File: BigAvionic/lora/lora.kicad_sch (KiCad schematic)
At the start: 0 parts

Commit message: add new power layer
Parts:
- added C43, C45: 100n, Capacitor_SMD:C_0805_2012Metric_Pad1.18x1.45mm_HandSolder, symbol Device:C
- added C44: 100u, Capacitor_SMD:C_0805_2012Metric_Pad1.18x1.45mm_HandSolder, symbol Device:C
- added C46: 22u, Capacitor_SMD:C_0805_2012Metric_Pad1.18x1.45mm_HandSolder, symbol Device:C
- added H1, H2, H3, H4: MountingHole, MountingHole:MountingHole_3.2mm_M3_DIN965_Pad, symbol Mechanical:MountingHole
- added R30, R31: 22ohm, Resistor_SMD:R_0805_2012Metric_Pad1.20x1.40mm_HandSolder, symbol Device:R
- added R32, R33: 10k, Resistor_SMD:R_0805_2012Metric_Pad1.20x1.40mm_HandSolder, symbol Device:R
- added U10: E22-400T30S, Tony:XCVR_E22-900T30S, symbol A_library:E22-XXXT30
- added U11: E80-900M23313S, Tony:E80-xxxM2213S, symbol A_library:E80-xxxM2213S
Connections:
- new net: R31.1, U10.4 (TXD)
- new net: R30.1, U10.5 (RXD)
- new net +3.3V: C43.1, C44.1, C45.1, C46.1, R32.2, R33.2, U10.2 (VCC), U11.25 (VCC)
- new net CSB_LORA920: U11.6 (NSS)
- new net GND: C43.2, C44.2, C45.2, C46.2, U10.1 (GND), U10.12 (GND), U10.13 (GND), U10.14 (GND), U10.23 (GND), U11.1 (GND), U11.19 (GND), U11.26 (GND), U11.8 (GND)
- new net LORA433_BUSY: U10.3 (AUX)
- new net LORA433_M0: U10.7 (M0)
- new net LORA433_M1: U10.6 (M1)
- new net LORA433_RST: R32.1, U10.22 (RESET)
- new net LORA920_BUSY: U11.7 (BUSY)
- new net LORA920_INT: U11.22 (DIO9)
- new net LORA920_RST: R33.1, U11.21 (LR_NRST)
- new net SPI3_MISO: U11.3 (MISO)
- new net SPI3_MOSI: U11.4 (MOSI)
- new net SPI3_SCK: U11.5 (SCK)
- new net UART3_RX: R31.2
- new net UART3_TX: R30.2
- no-connect marks 0 -> 8
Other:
- note added: "LORA 433"
- note added: "LORA 920"
- note added: "using ipx in the lora model"

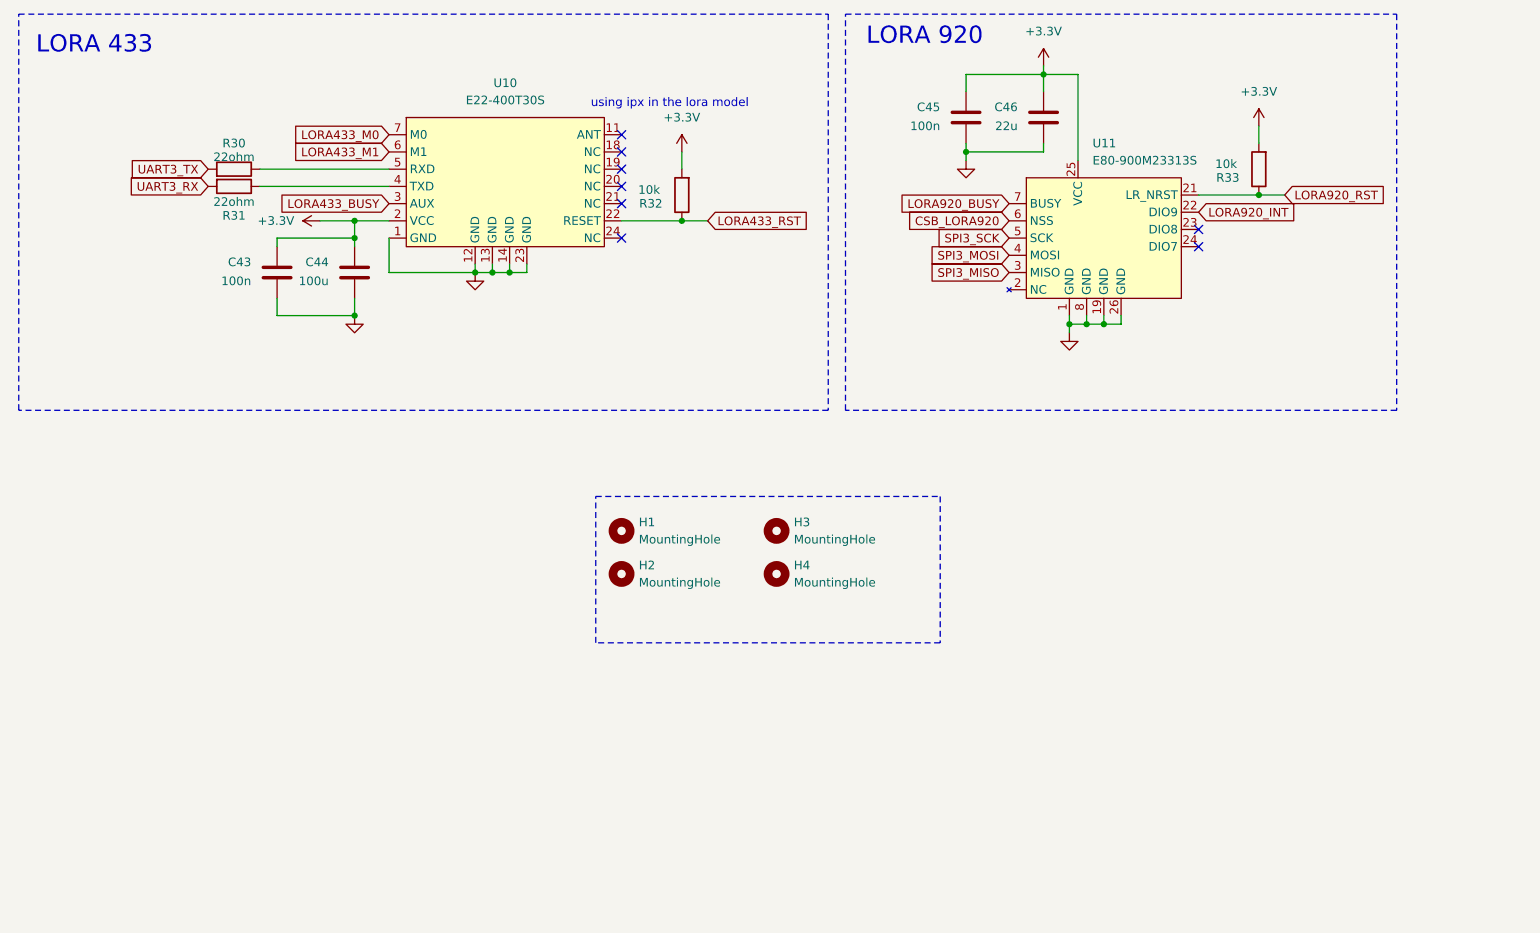
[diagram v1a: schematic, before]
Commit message: finish lora layer
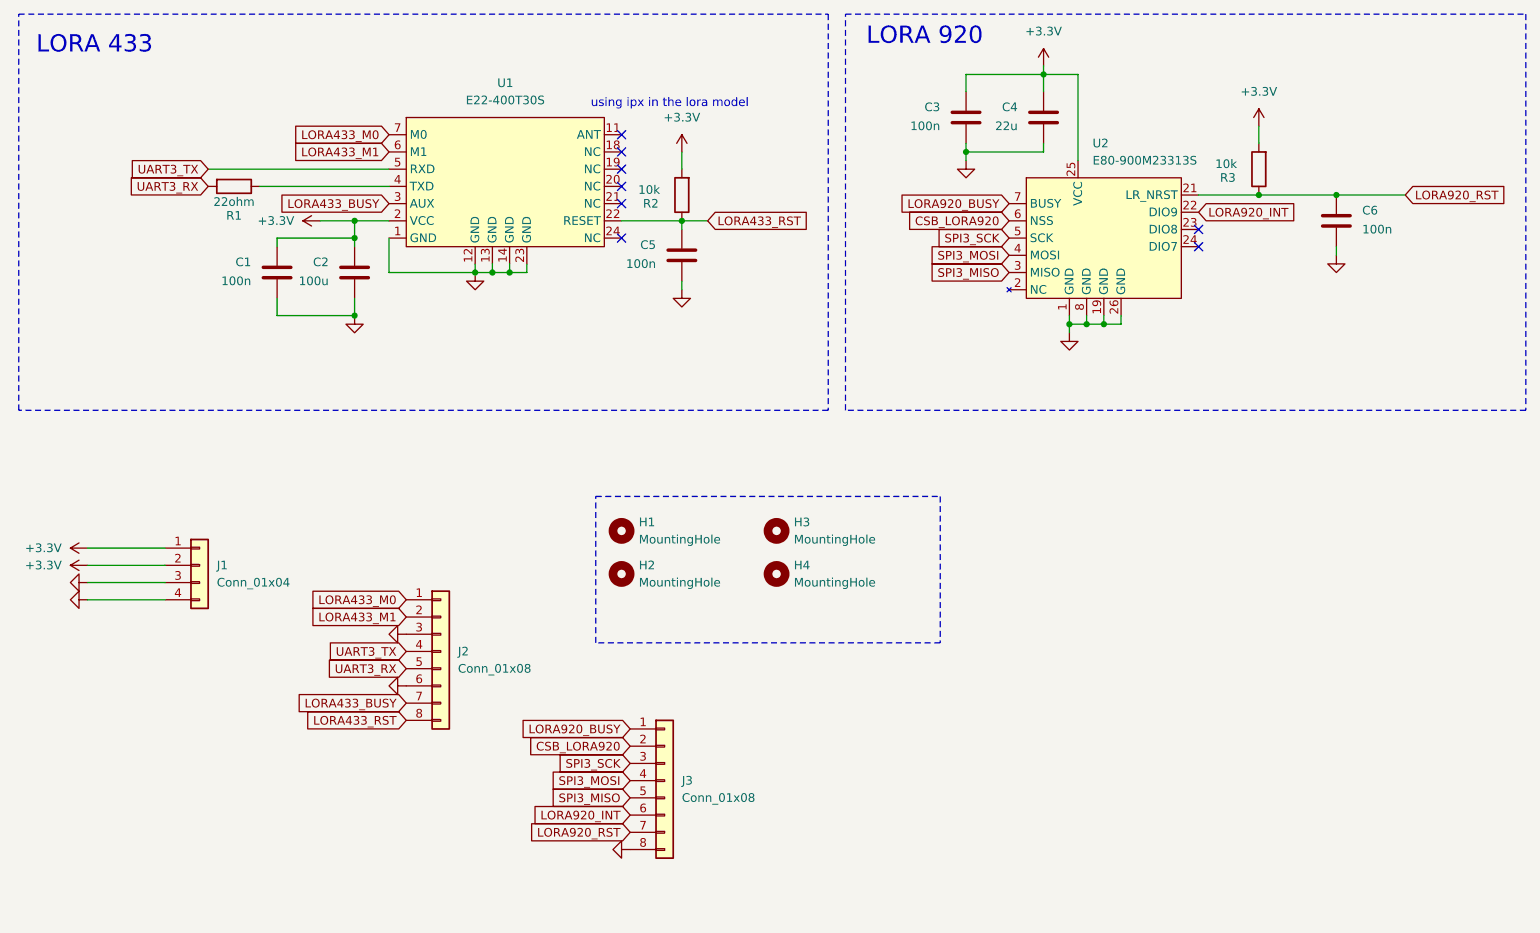
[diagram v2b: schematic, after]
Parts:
- removed R30: 22ohm, Resistor_SMD:R_0805_2012Metric_Pad1.20x1.40mm_HandSolder, symbol Device:R
- added C5, C6: 100n, Capacitor_SMD:C_0805_2012Metric_Pad1.18x1.45mm_HandSolder, symbol Device:C
- added J1: Conn_01x04, Connector_JST:JST_GH_SM04B-GHS-TB_1x04-1MP_P1.25mm_Horizontal, symbol Connector_Generic:Conn_01x04
- added J2, J3: Conn_01x08, Connector_JST:JST_GH_SM08B-GHS-TB_1x08-1MP_P1.25mm_Horizontal, symbol Connector_Generic:Conn_01x08
- renumbered C43 to C1, C44 to C2, C45 to C3, C46 to C4, R31 to R1, R32 to R2, R33 to R3, U10 to U1, U11 to U2
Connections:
- net +3.3V: now also J1.1 (Pin_1), J1.2 (Pin_2)
- net CSB_LORA920: now also J3.2 (Pin_2)
- net GND: now also C5.2, C6.2, J1.3 (Pin_3), J1.4 (Pin_4), J2.3 (Pin_3), J2.6 (Pin_6), J3.8 (Pin_8)
- net LORA433_BUSY: now also J2.7 (Pin_7)
- net LORA433_M0: now also J2.1 (Pin_1)
- net LORA433_M1: now also J2.2 (Pin_2)
- net LORA433_RST: now also C5.1, J2.8 (Pin_8)
- net LORA920_BUSY: now also J3.1 (Pin_1)
- net LORA920_INT: now also J3.6 (Pin_6)
- net LORA920_RST: now also C6.1, J3.7 (Pin_7)
- net SPI3_MISO: now also J3.5 (Pin_5)
- net SPI3_MOSI: now also J3.4 (Pin_4)
- net SPI3_SCK: now also J3.3 (Pin_3)
- net UART3_RX: now also J2.5 (Pin_5)
- net UART3_TX: now also U1.5 (RXD), J2.4 (Pin_4)

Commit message: finish lora & top
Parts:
- added 3V3, GND1: TestPoint, TestPoint:TestPoint_Pad_D1.0mm, symbol Connector:TestPoint
- added D1: RED_LED, LED_SMD:LED_0805_2012Metric_Pad1.15x1.40mm_HandSolder, symbol Device:LED
- added R4: 1k, Resistor_SMD:R_0805_2012Metric_Pad1.20x1.40mm_HandSolder, symbol Device:R
- renumbered C5 to C3, C3 to C4, C4 to C5
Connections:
- net +3.3V: now also 3V3.1, R4.2
- net GND: now also D1.1 (K), GND1.1
- new net: D1.2 (A), R4.1
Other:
- note added: "connectors"
- note added: "testpoint/LED"
- moved on the sheet: H1, H2, H3, H4, J1, J2, J3

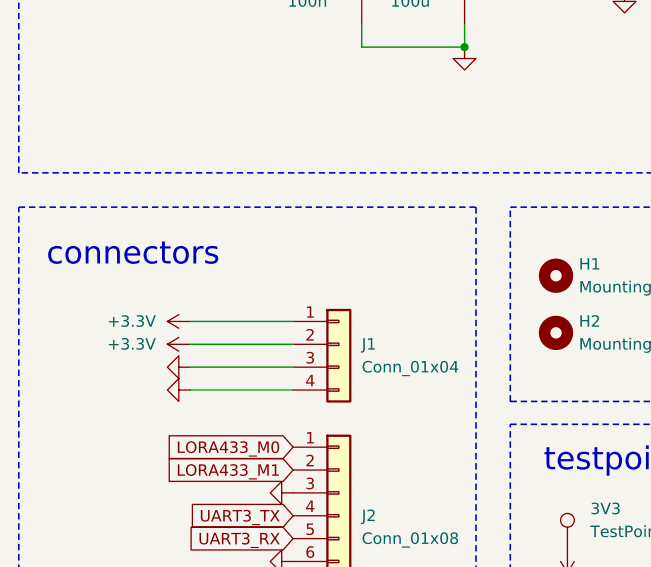
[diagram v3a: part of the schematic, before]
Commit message: check lora top power generate garber
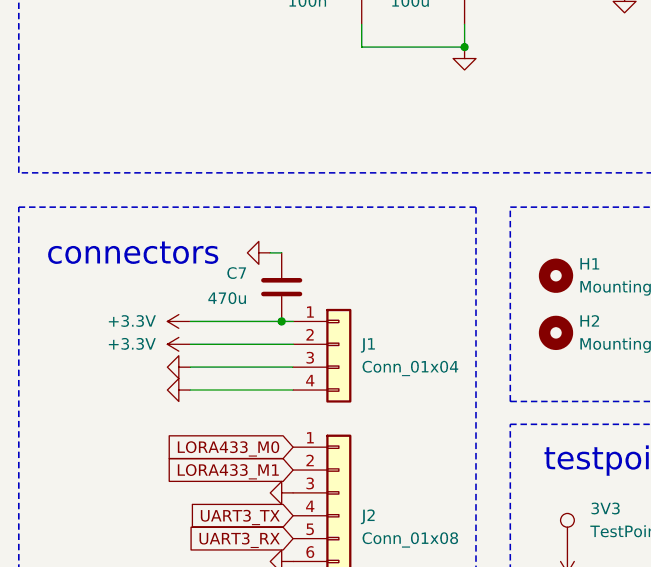
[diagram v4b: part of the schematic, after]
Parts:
- added C7: 470u, Capacitor_Tantalum_SMD:CP_EIA-7343-43_Kemet-X_HandSolder, symbol Device:C
- C2: footprint Capacitor_SMD:C_0805_2012Metric_Pad1.18x1.45mm_HandSolder -> Capacitor_Tantalum_SMD:CP_EIA-7343-31_Kemet-D_HandSolder
- C5: footprint Capacitor_SMD:C_0805_2012Metric_Pad1.18x1.45mm_HandSolder -> Capacitor_SMD:C_1206_3216Metric_Pad1.33x1.80mm_HandSolder
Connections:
- net +3.3V: now also C7.2
- net GND: now also C7.1
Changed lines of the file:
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@@
 	)
 	(junction
+		(at 78.74 134.62)
+		(diameter 0)
+		(color 0 0 0 0)
+	)
+	(junction
 		(at 99.06 90.17)
 		(diameter 0)
@@
 	(wire
 		(pts
-			(xy 80.01 134.62) (xy 68.58 134.62)
+			(xy 80.01 134.62) (xy 78.74 134.62)
 		)
 		(stroke
@@
 	(wire
 		(pts
+			(xy 77.47 127) (xy 78.74 127)
+		)
+		(stroke
+			(width 0)
+			(type default)
+		)
+	)
+	(wire
+		(pts
 			(xy 189.23 78.74) (xy 189.23 80.01)
 		)
@@
 	(wire
 		(pts
+			(xy 78.74 134.62) (xy 68.58 134.62)
+		)
+		(stroke
+			(width 0)
+			(type default)
+		)
+	)
+	(wire
+		(pts
 			(xy 104.14 97.79) (xy 116.84 97.79)
 		)
@@
 			)
 		)
-		(property "Footprint" "Capacitor_SMD:C_0805_2012Metric_Pad1.18x1.45mm_HandSolder"
+		(property "Footprint" "Capacitor_SMD:C_1206_3216Metric_Pad1.33x1.80mm_HandSolder"
 			(at 199.6948 78.74 0)
 			(effects
@@
 	)
 	(symbol
+		(lib_id "Device:C")
+		(at 78.74 130.81 0)
+		(mirror y)
+		(unit 1)
+		(exclude_from_sim no)
+		(in_bom yes)
+		(on_board yes)
+		(dnp no)
+		(property "Reference" "C7"
+			(at 74.93 129.286 0)
+			(effects
+				(font
+					(size 1.27 1.27)
+				)
+				(justify left)
+			)
+		)
+		(property "Value" "470u"
+			(at 74.93 132.0799 0)
+			(effects
+				(font
+					(size 1.27 1.27)
+				)
+				(justify left)
+			)
+		)
+		(property "Footprint" "Capacitor_Tantalum_SMD:CP_EIA-7343-43_Kemet-X_HandSolder"
+			(at 77.7748 134.62 0)
+			(effects
+				(font
+					(size 1.27 1.27)
+				)
+				(hide yes)
+			)
+		)
+		(property "Datasheet" "~"
+			(at 78.74 130.81 0)
+			(effects
+				(font
+					(size 1.27 1.27)
+				)
+				(hide yes)
+			)
+		)
+		(property "Description" "Unpolarized capacitor"
+			(at 78.74 130.81 0)
+			(effects
+				(font
+					(size 1.27 1.27)
+				)
+				(hide yes)
+			)
+		)
+		(pin "1"
+		)
+		(pin "2"
+		)
+		(instances
+			(project "lora"
+				(path "/e7e6f94f-519b-4ec5-b32e-6265e8eb4710"
+					(reference "C7")
+					(unit 1)
+				)
+			)
+		)
+	)
+	(symbol
 		(lib_id "power:GND")
 		(at 80.01 189.23 270)
@@
 	)
 	(symbol
+		(lib_id "power:GND")
+		(at 77.47 127 270)
+		(unit 1)
+		(exclude_from_sim no)
+		(in_bom yes)
+		(on_board yes)
+		(dnp no)
+		(property "Reference" "#PWR022"
+			(at 71.12 127 0)
+			(effects
+				(font
+					(size 1.27 1.27)
+				)
+				(hide yes)
+			)
+		)
+		(property "Value" "GND"
+			(at 72.39 127 0)
+			(effects
+				(font
+					(size 1.27 1.27)
+				)
+				(hide yes)
+			)
+		)
+		(property "Footprint" ""
+			(at 77.47 127 0)
+			(effects
+				(font
+					(size 1.27 1.27)
+				)
+				(hide yes)
+			)
+		)
+		(property "Datasheet" ""
+			(at 77.47 127 0)
+			(effects
+				(font
+					(size 1.27 1.27)
+				)
+				(hide yes)
+			)
+		)
+		(property "Description" "Power symbol creates a global label with name \"GND\" , ground"
+			(at 77.47 127 0)
+			(effects
+				(font
+					(size 1.27 1.27)
+				)
+				(hide yes)
+			)
+		)
+		(pin "1"
+		)
+		(instances
+			(project "lora"
+				(path "/e7e6f94f-519b-4ec5-b32e-6265e8eb4710"
+					(reference "#PWR022")
+					(unit 1)
+				)
+			)
+		)
+	)
+	(symbol
 		(lib_id "Device:C")
 		(at 87.63 97.79 0)
@@
 			)
 		)
-		(property "Footprint" "Capacitor_SMD:C_0805_2012Metric_Pad1.18x1.45mm_HandSolder"
+		(property "Footprint" "Capacitor_Tantalum_SMD:CP_EIA-7343-31_Kemet-D_HandSolder"
 			(at 98.0948 101.6 0)
 			(effects

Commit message: MCU process
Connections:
- net +3.3V: now also J1.3 (Pin_3), J1.4 (Pin_4); no longer J1.1 (Pin_1), J1.2 (Pin_2)
- net GND: now also J1.1 (Pin_1), J1.2 (Pin_2); no longer J1.3 (Pin_3), J1.4 (Pin_4)
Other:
- moved on the sheet: C7, J1
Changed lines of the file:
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@@
 	)
 	(junction
-		(at 78.74 134.62)
+		(at 78.74 138.43)
 		(diameter 0)
 		(color 0 0 0 0)
@@
 	(wire
 		(pts
-			(xy 80.01 134.62) (xy 78.74 134.62)
-		)
-		(stroke
-			(width 0)
-			(type default)
-		)
-	)
-	(wire
-		(pts
 			(xy 207.01 104.14) (xy 207.01 105.41)
 		)
@@
 	(wire
 		(pts
-			(xy 77.47 127) (xy 78.74 127)
+			(xy 80.01 135.89) (xy 68.58 135.89)
 		)
 		(stroke
@@
 	(wire
 		(pts
+			(xy 80.01 130.81) (xy 68.58 130.81)
+		)
+		(stroke
+			(width 0)
+			(type default)
+		)
+	)
+	(wire
+		(pts
+			(xy 77.47 146.05) (xy 78.74 146.05)
+		)
+		(stroke
+			(width 0)
+			(type default)
+		)
+	)
+	(wire
+		(pts
 			(xy 87.63 92.71) (xy 99.06 92.71)
 		)
@@
 	(wire
 		(pts
-			(xy 80.01 142.24) (xy 68.58 142.24)
+			(xy 78.74 138.43) (xy 68.58 138.43)
 		)
 		(stroke
@@
 	(wire
 		(pts
-			(xy 124.46 97.79) (xy 121.92 97.79)
+			(xy 80.01 138.43) (xy 78.74 138.43)
 		)
 		(stroke
@@
 	(wire
 		(pts
-			(xy 189.23 80.01) (xy 189.23 81.28)
+			(xy 124.46 97.79) (xy 121.92 97.79)
 		)
 		(stroke
@@
 	(wire
 		(pts
-			(xy 104.14 92.71) (xy 104.14 97.79)
+			(xy 189.23 80.01) (xy 189.23 81.28)
 		)
 		(stroke
@@
 	(wire
 		(pts
-			(xy 87.63 104.14) (xy 99.06 104.14)
+			(xy 104.14 92.71) (xy 104.14 97.79)
 		)
 		(stroke
@@
 	(wire
 		(pts
-			(xy 124.46 96.52) (xy 124.46 97.79)
+			(xy 87.63 104.14) (xy 99.06 104.14)
 		)
 		(stroke
@@
 	(wire
 		(pts
-			(xy 80.01 137.16) (xy 68.58 137.16)
+			(xy 124.46 96.52) (xy 124.46 97.79)
 		)
 		(stroke
@@
 	(wire
 		(pts
-			(xy 99.06 90.17) (xy 104.14 90.17)
+			(xy 80.01 133.35) (xy 68.58 133.35)
 		)
 		(stroke
@@
 	(wire
 		(pts
-			(xy 93.98 90.17) (xy 99.06 90.17)
+			(xy 99.06 90.17) (xy 104.14 90.17)
 		)
 		(stroke
@@
 	(wire
 		(pts
-			(xy 212.09 105.41) (xy 209.55 105.41)
+			(xy 93.98 90.17) (xy 99.06 90.17)
 		)
 		(stroke
@@
 	(wire
 		(pts
-			(xy 204.47 105.41) (xy 207.01 105.41)
+			(xy 212.09 105.41) (xy 209.55 105.41)
 		)
 		(stroke
@@
 	(wire
 		(pts
-			(xy 77.47 82.55) (xy 104.14 82.55)
+			(xy 204.47 105.41) (xy 207.01 105.41)
 		)
 		(stroke
@@
 	(wire
 		(pts
-			(xy 207.01 105.41) (xy 209.55 105.41)
+			(xy 77.47 82.55) (xy 104.14 82.55)
 		)
 		(stroke
@@
 	(wire
 		(pts
-			(xy 80.01 139.7) (xy 68.58 139.7)
+			(xy 207.01 105.41) (xy 209.55 105.41)
 		)
 		(stroke
@@
 	(wire
 		(pts
-			(xy 78.74 134.62) (xy 68.58 134.62)
-		)
-		(stroke
-			(width 0)
-			(type default)
-		)
-	)
-	(wire
-		(pts
 			(xy 104.14 97.79) (xy 116.84 97.79)
 		)
@@
 	(symbol
 		(lib_id "power:+3.3V")
-		(at 68.58 134.62 90)
-		(mirror x)
+		(at 68.58 138.43 90)
 		(unit 1)
 		(exclude_from_sim no)
@@
 		(fields_autoplaced yes)
 		(property "Reference" "#PWR01"
-			(at 72.39 134.62 0)
+			(at 72.39 138.43 0)
 			(effects
 				(font
@@
 		)
 		(property "Value" "+3.3V"
-			(at 64.77 134.6199 90)
+			(at 64.77 138.4301 90)
 			(effects
 				(font
@@
 		)
 		(property "Footprint" ""
-			(at 68.58 134.62 0)
+			(at 68.58 138.43 0)
 			(effects
 				(font
@@
 		)
 		(property "Datasheet" ""
-			(at 68.58 134.62 0)
+			(at 68.58 138.43 0)
 			(effects
 				(font
@@
 		)
 		(property "Description" "Power symbol creates a global label with name \"+3.3V\""
-			(at 68.58 134.62 0)
+			(at 68.58 138.43 0)
 			(effects
 				(font
@@
 	(symbol
 		(lib_id "power:GND")
-		(at 68.58 142.24 270)
+		(at 68.58 130.81 270)
+		(mirror x)
 		(unit 1)
 		(exclude_from_sim no)
@@
 		(dnp no)
 		(property "Reference" "#PWR04"
-			(at 62.23 142.24 0)
+			(at 62.23 130.81 0)
 			(effects
 				(font
@@
 		)
 		(property "Value" "GND"
-			(at 63.5 142.24 0)
+			(at 63.5 130.81 0)
 			(effects
 				(font
@@
 		)
 		(property "Footprint" ""
-			(at 68.58 142.24 0)
+			(at 68.58 130.81 0)
 			(effects
 				(font
@@
 		)
 		(property "Datasheet" ""
-			(at 68.58 142.24 0)
+			(at 68.58 130.81 0)
 			(effects
 				(font
@@
 		)
 		(property "Description" "Power symbol creates a global label with name \"GND\" , ground"
-			(at 68.58 142.24 0)
+			(at 68.58 130.81 0)
 			(effects
 				(font
@@
 	(symbol
 		(lib_id "power:+3.3V")
-		(at 68.58 137.16 90)
-		(mirror x)
+		(at 68.58 135.89 90)
 		(unit 1)
 		(exclude_from_sim no)
@@
 		(fields_autoplaced yes)
 		(property "Reference" "#PWR02"
-			(at 72.39 137.16 0)
+			(at 72.39 135.89 0)
 			(effects
 				(font
@@
 		)
 		(property "Value" "+3.3V"
-			(at 64.77 137.1599 90)
+			(at 64.77 135.8901 90)
 			(effects
 				(font
@@
 		)
 		(property "Footprint" ""
-			(at 68.58 137.16 0)
+			(at 68.58 135.89 0)
 			(effects
 				(font
@@
 		)
 		(property "Datasheet" ""
-			(at 68.58 137.16 0)
+			(at 68.58 135.89 0)
 			(effects
 				(font
@@
 		)
 		(property "Description" "Power symbol creates a global label with name \"+3.3V\""
-			(at 68.58 137.16 0)
+			(at 68.58 135.89 0)
 			(effects
 				(font
@@
 	(symbol
 		(lib_id "Device:C")
-		(at 78.74 130.81 0)
-		(mirror y)
+		(at 78.74 142.24 180)
 		(unit 1)
 		(exclude_from_sim no)
@@
 		(dnp no)
 		(property "Reference" "C7"
-			(at 74.93 129.286 0)
+			(at 74.93 143.764 0)
 			(effects
 				(font
@@
 		)
 		(property "Value" "470u"
-			(at 74.93 132.0799 0)
+			(at 74.93 140.9701 0)
 			(effects
 				(font
@@
 		)
 		(property "Footprint" "Capacitor_Tantalum_SMD:CP_EIA-7343-43_Kemet-X_HandSolder"
-			(at 77.7748 134.62 0)
+			(at 77.7748 138.43 0)
 			(effects
 				(font
@@
 		)
 		(property "Datasheet" "~"
-			(at 78.74 130.81 0)
+			(at 78.74 142.24 0)
 			(effects
 				(font
@@
 		)
 		(property "Description" "Unpolarized capacitor"
-			(at 78.74 130.81 0)
+			(at 78.74 142.24 0)
 			(effects
 				(font
@@
 	(symbol
 		(lib_id "Connector_Generic:Conn_01x04")
-		(at 85.09 137.16 0)
+		(at 85.09 133.35 0)
 		(unit 1)
 		(exclude_from_sim no)
@@
 		(fields_autoplaced yes)
 		(property "Reference" "J1"
-			(at 87.63 137.1599 0)
+			(at 87.63 133.3499 0)
 			(effects
 				(font
@@
 		)
 		(property "Value" "Conn_01x04"
-			(at 87.63 139.6999 0)
+			(at 87.63 135.8899 0)
 			(effects
 				(font
@@
 		)
 		(property "Footprint" "Connector_JST:JST_GH_SM04B-GHS-TB_1x04-1MP_P1.25mm_Horizontal"
-			(at 85.09 137.16 0)
+			(at 85.09 133.35 0)
 			(effects
 				(font
@@
 		)
 		(property "Datasheet" "~"
-			(at 85.09 137.16 0)
+			(at 85.09 133.35 0)
 			(effects
 				(font
@@
 		)
 		(property "Description" "Generic connector, single row, 01x04, script generated (kicad-library-utils/schlib/autogen/connector/)"
-			(at 85.09 137.16 0)
+			(at 85.09 133.35 0)
 			(effects
 				(font
@@
 	(symbol
 		(lib_id "power:GND")
-		(at 77.47 127 270)
+		(at 77.47 146.05 270)
+		(mirror x)
 		(unit 1)
 		(exclude_from_sim no)
@@
 		(dnp no)
 		(property "Reference" "#PWR022"
-			(at 71.12 127 0)
+			(at 71.12 146.05 0)
 			(effects
 				(font
@@
 		)
 		(property "Value" "GND"
-			(at 72.39 127 0)
+			(at 72.39 146.05 0)
 			(effects
 				(font
@@
 		)
 		(property "Footprint" ""
-			(at 77.47 127 0)
+			(at 77.47 146.05 0)
 			(effects
 				(font
@@
 		)
 		(property "Datasheet" ""
-			(at 77.47 127 0)
+			(at 77.47 146.05 0)
 			(effects
 				(font
@@
 		)
 		(property "Description" "Power symbol creates a global label with name \"GND\" , ground"
-			(at 77.47 127 0)
+			(at 77.47 146.05 0)
 			(effects
 				(font
@@
 	(symbol
 		(lib_id "power:GND")
-		(at 68.58 139.7 270)
+		(at 68.58 133.35 270)
+		(mirror x)
 		(unit 1)
 		(exclude_from_sim no)
@@
 		(dnp no)
 		(property "Reference" "#PWR03"
-			(at 62.23 139.7 0)
+			(at 62.23 133.35 0)
 			(effects
 				(font
@@
 		)
 		(property "Value" "GND"
-			(at 63.5 139.7 0)
+			(at 63.5 133.35 0)
 			(effects
 				(font
@@
 		)
 		(property "Footprint" ""
-			(at 68.58 139.7 0)
+			(at 68.58 133.35 0)
 			(effects
 				(font
@@
 		)
 		(property "Datasheet" ""
-			(at 68.58 139.7 0)
+			(at 68.58 133.35 0)
 			(effects
 				(font
@@
 		)
 		(property "Description" "Power symbol creates a global label with name \"GND\" , ground"
-			(at 68.58 139.7 0)
+			(at 68.58 133.35 0)
 			(effects
 				(font
